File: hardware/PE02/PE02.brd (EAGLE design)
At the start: 25.4 x 27.3 mm, 29 parts, among them IC1 MSP430G2231, IC2 TPS78222, J1 78171-0002, T1 BC846

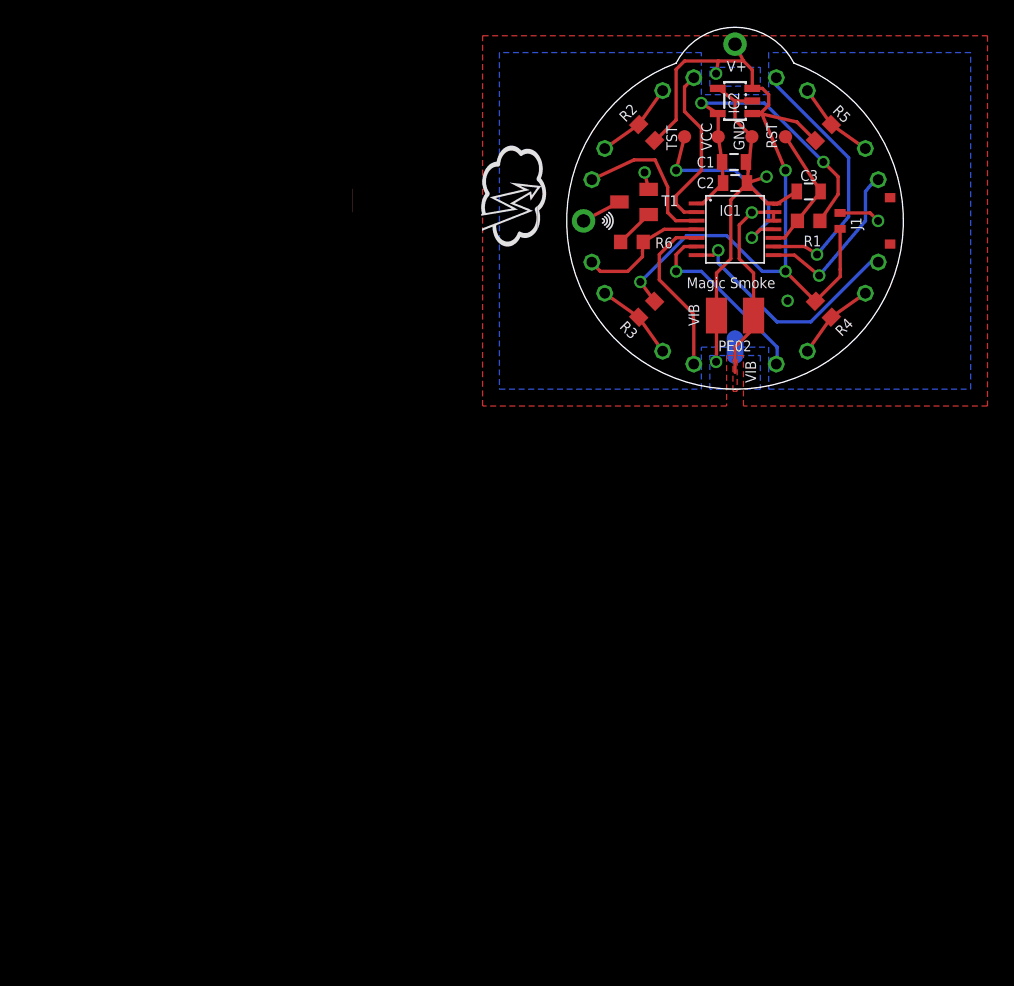
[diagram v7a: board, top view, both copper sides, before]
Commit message: PE02 order from OSHpark
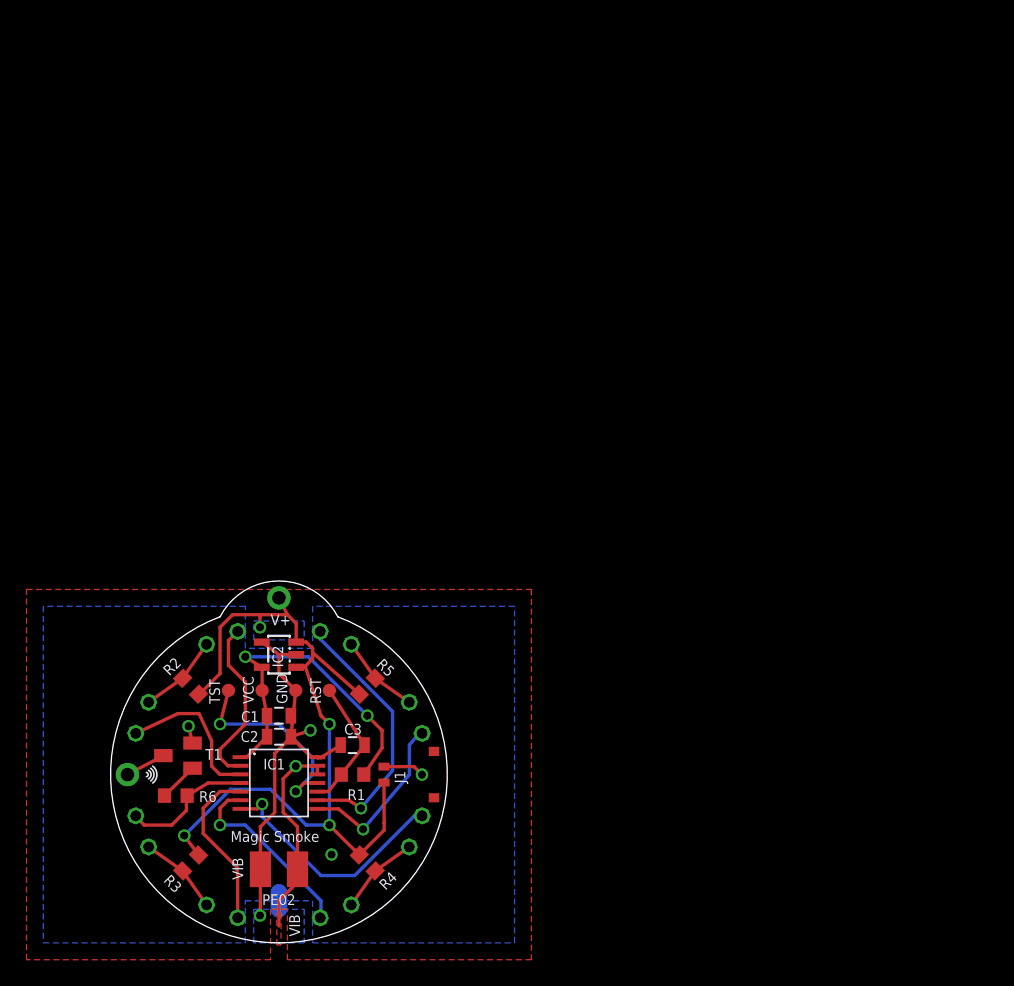
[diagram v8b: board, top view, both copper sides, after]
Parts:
- moved C2 54.1 mm to (16.4, 17.0)
- moved C3 54.1 mm to (21.9, 16.3)
- moved D1 54.1 mm to (12.1, 24.4)
- moved D2 54.1 mm to (6.06, 18.4)
- moved D3 54.1 mm to (6.06, 9.81)
- moved D4 54.1 mm to (12.1, 3.78)
- moved D5 54.1 mm to (20.7, 3.78)
- moved D6 54.1 mm to (26.7, 9.81)
- moved D7 54.1 mm to (26.7, 18.4)
- moved D8 54.1 mm to (20.7, 24.4)
- moved GND 54.1 mm to (17.7, 20.4)
- moved IC1 54.1 mm to (16.4, 13.5)
- moved J1 54.1 mm to (26.4, 14.1)
- moved JP2 54.1 mm to (16.4, 27.4)
- moved MVS0608.02 54.1 mm to (16.4, 6.95)
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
